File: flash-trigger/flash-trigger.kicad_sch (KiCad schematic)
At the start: 32 parts, among them J1 TRIG, J2 GND, Q1 NDS331N, SW1 PCM12, SW2 Bat Test, U1 74LV123, U2 BD48K27G

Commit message: Fixes and improvements
 * fix the preflash detection
 * clean the canon hot shoe schematics up
 * enlarge the hotshoe pcb and place two new mounting pins
 * change the battery low to a battery good detection
 * move the supervisor ic away from the hot shoe rail
 * use a longer pogo pin
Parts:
- removed U2: BD48K27G, Package_TO_SOT_SMD:SOT-23_Handsoldering, symbol Power_Management:BD48KxxG
- added J3, J4: GND, Connector_MillMax:0508_20mil, symbol Connector_Pin:Pin
- added U2: BD49KxxG, Package_TO_SOT_SMD:SOT-23_Handsoldering, symbol Power_Management:BD49KxxG
- D6: value RED -> GREEN
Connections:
- net +3V0: no longer D6.2 (A), U1.2 (B)
- net GND: now also D6.1 (K), U1.1 (A), J3.1 (Pin_1), J4.1 (Pin_1), U2.1 (GND)
- net TRIG: now also U1.2 (B); no longer U1.1 (A)
- net at R11.1: now also D6.2 (A); no longer D6.1 (K)
- net at R11.2: now also U2.2 (VOUT)
- net at R13.1, SW2.2: now also U2.3 (VDD)
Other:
- moved on the sheet: BT1, C2, C3, D6

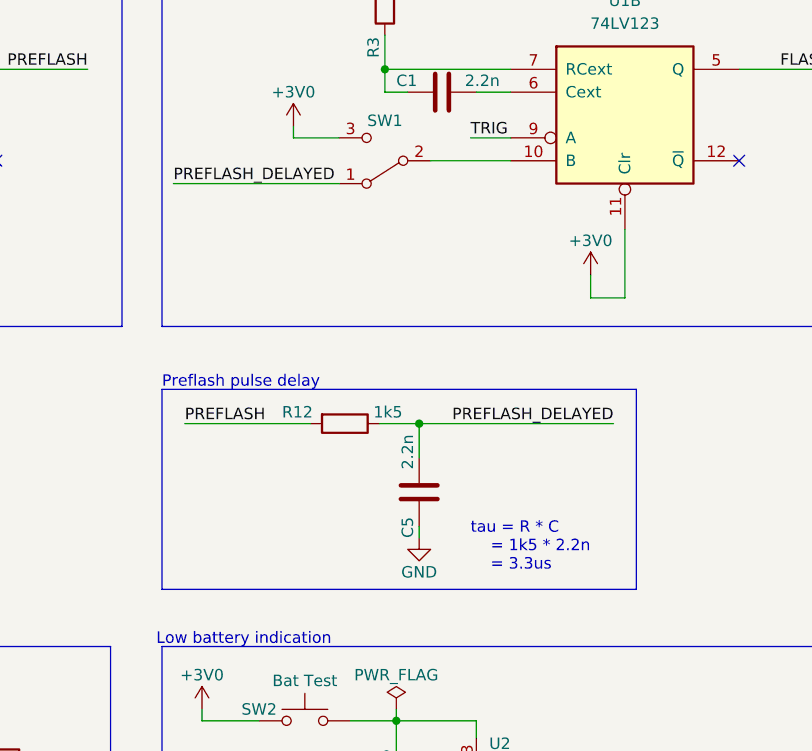
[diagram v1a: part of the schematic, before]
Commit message: flash-trigger: Drop RC circuit and improve layout
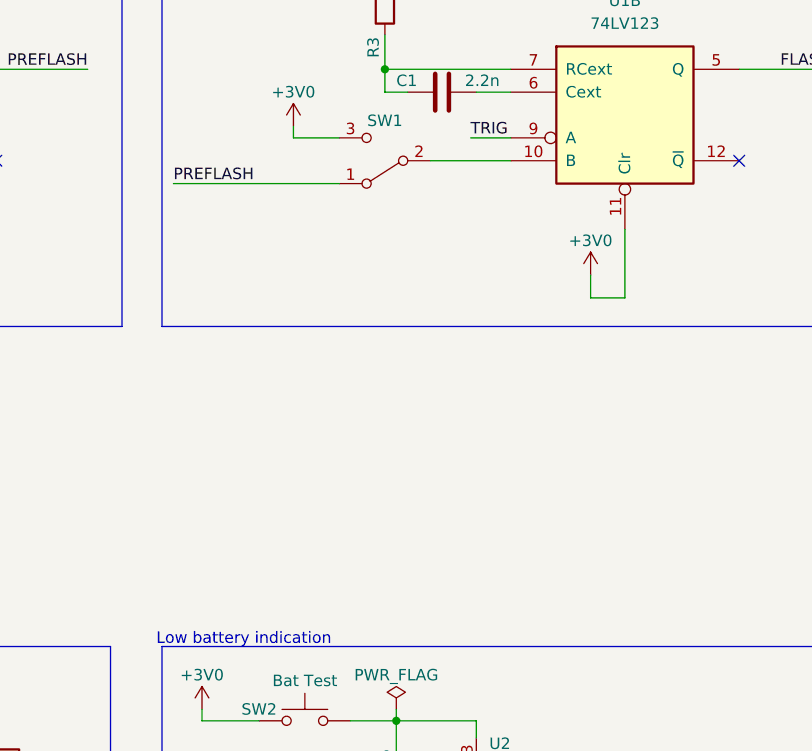
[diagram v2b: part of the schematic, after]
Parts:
- removed C5: 2.2n, Capacitor_SMD:C_0603_1608Metric_Pad1.08x0.95mm_HandSolder, symbol Device:C
- removed R12: 1k5, Resistor_SMD:R_0603_1608Metric_Pad0.98x0.95mm_HandSolder, symbol Device:R
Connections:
- net PREFLASH_DELAYED is gone; now on net PREFLASH: SW1.1 (A)
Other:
- note removed: "Preflash pulse delay"
- note removed: "tau = R * C = 1k5 * 2.2n = 3.3us"
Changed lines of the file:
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@@
   (junction (at 60.96 142.24) (diameter 0) (color 0 0 0 0)
-  )
-  (junction (at 142.875 93.98) (diameter 0) (color 0 0 0 0)
   )
   (junction (at 55.245 127.635) (diameter 0) (color 0 0 0 0)
@@
     (stroke (width 0) (type default) (color 0 0 0 0))
   )
-  (polyline (pts (xy 114.3 90.17) (xy 114.3 112.395))
-    (stroke (width 0) (type default) (color 0 0 0 0))
-  )
   (wire (pts (xy 245.11 49.53) (xy 245.11 57.15))
     (stroke (width 0) (type default) (color 0 0 0 0))
@@
     (stroke (width 0) (type default) (color 0 0 0 0))
   )
-  (wire (pts (xy 142.875 93.98) (xy 164.465 93.98))
-    (stroke (width 0) (type default) (color 0 0 0 0))
-  )
-  (wire (pts (xy 142.875 97.79) (xy 142.875 93.98))
-    (stroke (width 0) (type default) (color 0 0 0 0))
-  )
   (polyline (pts (xy 200.025 151.13) (xy 114.3 151.13))
     (stroke (width 0) (type default) (color 0 0 0 0))
@@
     (stroke (width 0) (type default) (color 0 0 0 0))
   )
-  (polyline (pts (xy 114.3 90.17) (xy 167.005 90.17))
-    (stroke (width 0) (type default) (color 0 0 0 0))
-  )
   (wire (pts (xy 79.375 77.47) (xy 79.375 80.01))
     (stroke (width 0) (type default) (color 0 0 0 0))
   )
-  (wire (pts (xy 142.875 105.41) (xy 142.875 106.68))
-    (stroke (width 0) (type default) (color 0 0 0 0))
-  )
   (wire (pts (xy 55.245 127.635) (xy 55.245 131.445))
     (stroke (width 0) (type default) (color 0 0 0 0))
@@
     (stroke (width 0) (type default) (color 0 0 0 0))
   )
-  (wire (pts (xy 138.43 93.98) (xy 142.875 93.98))
-    (stroke (width 0) (type default) (color 0 0 0 0))
-  )
   (wire (pts (xy 153.035 54.61) (xy 139.065 54.61))
     (stroke (width 0) (type default) (color 0 0 0 0))
@@
     (stroke (width 0) (type default) (color 0 0 0 0))
   )
-  (wire (pts (xy 116.84 93.98) (xy 130.81 93.98))
-    (stroke (width 0) (type default) (color 0 0 0 0))
-  )
   (polyline (pts (xy 15.24 195.58) (xy 99.06 195.58))
     (stroke (width 0) (type default) (color 0 0 0 0))
@@
     (stroke (width 0) (type default) (color 0 0 0 0))
   )
-  (polyline (pts (xy 114.3 112.395) (xy 167.005 112.395))
-    (stroke (width 0) (type default) (color 0 0 0 0))
-  )
   (wire (pts (xy 67.31 124.46) (xy 67.31 127.635))
     (stroke (width 0) (type default) (color 0 0 0 0))
@@
   )
   (wire (pts (xy 56.515 36.195) (xy 56.515 43.18))
-    (stroke (width 0) (type default) (color 0 0 0 0))
-  )
-  (polyline (pts (xy 167.005 90.17) (xy 167.005 112.395))
     (stroke (width 0) (type default) (color 0 0 0 0))
   )
@@
   )
   (text "Low battery indication" (at 113.665 118.745 0)
-    (effects (font (size 1.27 1.27)) (justify left bottom))
-  )
-  (text "tau = R * C\n    = 1k5 * 2.2n\n    = 3.3us" (at 148.59 110.49 0)
     (effects (font (size 1.27 1.27)) (justify left bottom))
   )
@@
     (effects (font (size 1.27 1.27)) (justify left bottom))
   )
-  (text "Preflash pulse delay" (at 114.3 90.17 0)
-    (effects (font (size 1.27 1.27)) (justify left bottom))
-  )
   (label "TRIG" (at 66.04 64.77 0)
     (effects (font (size 1.27 1.27)) (justify left bottom))
   )
-  (label "PREFLASH_DELAYED" (at 164.465 93.98 180)
-    (effects (font (size 1.27 1.27)) (justify right bottom))
-  )
   (label "TRIG" (at 148.59 62.23 0)
     (effects (font (size 1.27 1.27)) (justify left bottom))
   )
-  (label "PREFLASH_DELAYED" (at 115.57 67.31 0)
-    (effects (font (size 1.27 1.27)) (justify left bottom))
-  )
-  (label "PREFLASH" (at 116.84 93.98 0)
+  (label "PREFLASH" (at 115.57 67.31 0)
     (effects (font (size 1.27 1.27)) (justify left bottom))
   )
@@
     )
     (pin "1")
-  )
-  (symbol (lib_id "Device:R") (at 134.62 93.98 270) (unit 1)
-    (in_bom yes) (on_board yes)
-    (property "Reference" "R12" (id 0) (at 127.635 92.71 90)
-      (effects (font (size 1.27 1.27)) (justify left))
-    )
-    (property "Value" "1k5" (id 1) (at 137.795 92.71 90)
-      (effects (font (size 1.27 1.27)) (justify left))
-    )
-    (property "Footprint" "Resistor_SMD:R_0603_1608Metric_Pad0.98x0.95mm_HandSolder" (id 2) (at 134.62 92.202 90)
-      (effects (font (size 1.27 1.27)) hide)
-    )
-    (property "Datasheet" "~" (id 3) (at 134.62 93.98 0)
-      (effects (font (size 1.27 1.27)) hide)
-    )
-    (pin "1")
-    (pin "2")
   )
   (symbol (lib_id "Device:C") (at 62.865 57.15 270) (unit 1)
@@
     (pin "8")
   )
-  (symbol (lib_id "power:GND") (at 142.875 106.68 0) (unit 1)
-    (in_bom yes) (on_board yes)
-    (property "Reference" "#PWR02" (id 0) (at 142.875 113.03 0)
-      (effects (font (size 1.27 1.27)) hide)
-    )
-    (property "Value" "GND" (id 1) (at 142.875 110.49 0))
-    (property "Footprint" "" (id 2) (at 142.875 106.68 0)
-      (effects (font (size 1.27 1.27)) hide)
-    )
-    (property "Datasheet" "" (id 3) (at 142.875 106.68 0)
-      (effects (font (size 1.27 1.27)) hide)
-    )
-    (pin "1")
-  )
   (symbol (lib_id "Device:R") (at 224.79 74.93 90) (unit 1)
     (in_bom yes) (on_board yes)
@@
     )
     (pin "1")
-  )
-  (symbol (lib_id "Device:C") (at 142.875 101.6 0) (unit 1)
-    (in_bom yes) (on_board yes)
-    (property "Reference" "C5" (id 0) (at 141.605 106.68 90)
-      (effects (font (size 1.27 1.27)) (justify left))
-    )
-    (property "Value" "2.2n" (id 1) (at 141.605 99.06 90)
-      (effects (font (size 1.27 1.27)) (justify left))
-    )
-    (property "Footprint" "Capacitor_SMD:C_0603_1608Metric_Pad1.08x0.95mm_HandSolder" (id 2) (at 143.8402 105.41 0)
-      (effects (font (size 1.27 1.27)) hide)
-    )
-    (property "Datasheet" "~" (id 3) (at 142.875 101.6 0)
-      (effects (font (size 1.27 1.27)) hide)
-    )
-    (pin "1")
-    (pin "2")
   )
   (symbol (lib_id "power:GND") (at 194.945 138.43 0) (unit 1)
@@
       (reference "#PWR01") (unit 1) (value "GND") (footprint "")
     )
-    (path "/7525ff0d-7040-4ba5-9383-b2716010d0ab"
-      (reference "#PWR02") (unit 1) (value "GND") (footprint "")
-    )
     (path "/45240cf5-fa14-449b-8df8-95cb2ab631a1"
       (reference "#PWR03") (unit 1) (value "GND") (footprint "")
@@
       (reference "C4") (unit 1) (value "220n") (footprint "Capacitor_SMD:C_0603_1608Metric_Pad1.08x0.95mm_HandSolder")
     )
-    (path "/e5cffcd4-8c81-4263-b9d9-fc1257ee69ce"
-      (reference "C5") (unit 1) (value "2.2n") (footprint "Capacitor_SMD:C_0603_1608Metric_Pad1.08x0.95mm_HandSolder")
-    )
     (path "/412c51c3-a4b0-43de-9409-a8b70956267a"
       (reference "D1") (unit 1) (value "RED") (footprint "LED_THT:LED_D5.0mm_Horizontal_O3.81mm_Z3.0mm")
@@
       (reference "R11") (unit 1) (value "1k5") (footprint "Resistor_SMD:R_0603_1608Metric_Pad0.98x0.95mm_HandSolder")
     )
-    (path "/1aa0f7e1-6ed5-404c-ba9b-a644e163f5fb"
-      (reference "R12") (unit 1) (value "1k5") (footprint "Resistor_SMD:R_0603_1608Metric_Pad0.98x0.95mm_HandSolder")
-    )
     (path "/9efe46b7-7144-40b9-a143-1703b8afb1fc"

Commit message: Renumber RefDes and add OSHW logo and URL
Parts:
- renumbered C2 to C1, C3 to C2, C4 to C3, C1 to C4, R3 to R10, R13 to R12, R7 to R3, R8 to R4, R9 to R5, R4 to R6, R5 to R7, R6 to R8, R10 to R9
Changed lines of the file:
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@@
   (symbol (lib_id "Device:C") (at 62.865 57.15 270) (unit 1)
     (in_bom yes) (on_board yes)
-    (property "Reference" "C4" (id 0) (at 57.785 55.88 90)
+    (property "Reference" "C3" (id 0) (at 57.785 55.88 90)
       (effects (font (size 1.27 1.27)) (justify left))
     )
@@
   (symbol (lib_id "Device:C") (at 145.415 57.15 270) (unit 1)
     (in_bom yes) (on_board yes)
-    (property "Reference" "C1" (id 0) (at 140.335 55.88 90)
+    (property "Reference" "C4" (id 0) (at 140.335 55.88 90)
       (effects (font (size 1.27 1.27)) (justify left))
     )
@@
   (symbol (lib_id "Device:R") (at 260.35 60.96 0) (unit 1)
     (in_bom yes) (on_board yes)
-    (property "Reference" "R8" (id 0) (at 259.08 66.675 90)
+    (property "Reference" "R4" (id 0) (at 259.08 66.675 90)
       (effects (font (size 1.27 1.27)) (justify left))
     )
@@
   (symbol (lib_id "Device:R") (at 234.95 83.82 0) (unit 1)
     (in_bom yes) (on_board yes)
-    (property "Reference" "R5" (id 0) (at 233.68 89.535 90)
+    (property "Reference" "R7" (id 0) (at 233.68 89.535 90)
       (effects (font (size 1.27 1.27)) (justify left))
     )
@@
   (symbol (lib_id "Device:R") (at 224.79 74.93 90) (unit 1)
     (in_bom yes) (on_board yes)
-    (property "Reference" "R4" (id 0) (at 219.71 73.66 90))
+    (property "Reference" "R6" (id 0) (at 219.71 73.66 90))
     (property "Value" "22R" (id 1) (at 229.87 73.66 90))
     (property "Footprint" "Resistor_SMD:R_0603_1608Metric_Pad0.98x0.95mm_HandSolder" (id 2) (at 224.79 76.708 90)
@@
   (symbol (lib_id "Device:C") (at 60.96 135.255 0) (unit 1)
     (in_bom yes) (on_board yes)
-    (property "Reference" "C2" (id 0) (at 59.69 140.335 90)
+    (property "Reference" "C1" (id 0) (at 59.69 140.335 90)
       (effects (font (size 1.27 1.27)) (justify left))
     )
@@
   (symbol (lib_id "Device:C") (at 67.31 135.255 0) (unit 1)
     (in_bom yes) (on_board yes)
-    (property "Reference" "C3" (id 0) (at 66.04 140.335 90)
+    (property "Reference" "C2" (id 0) (at 66.04 140.335 90)
       (effects (font (size 1.27 1.27)) (justify left))
     )
@@
   (symbol (lib_id "Device:R") (at 140.335 136.525 0) (unit 1)
     (in_bom yes) (on_board yes)
-    (property "Reference" "R13" (id 0) (at 139.065 143.51 90)
+    (property "Reference" "R12" (id 0) (at 139.065 143.51 90)
       (effects (font (size 1.27 1.27)) (justify left))
     )
@@
   (symbol (lib_id "Device:R") (at 265.43 60.96 0) (unit 1)
     (in_bom yes) (on_board yes)
-    (property "Reference" "R9" (id 0) (at 264.16 66.675 90)
+    (property "Reference" "R5" (id 0) (at 264.16 66.675 90)
       (effects (font (size 1.27 1.27)) (justify left))
     )
@@
   (symbol (lib_id "Device:R") (at 255.27 60.96 0) (unit 1)
     (in_bom yes) (on_board yes)
-    (property "Reference" "R7" (id 0) (at 254 66.675 90)
+    (property "Reference" "R3" (id 0) (at 254 66.675 90)
       (effects (font (size 1.27 1.27)) (justify left))
     )
@@
   (symbol (lib_id "Device:R") (at 139.065 46.99 180) (unit 1)
     (in_bom yes) (on_board yes)
-    (property "Reference" "R3" (id 0) (at 137.795 53.34 90)
+    (property "Reference" "R10" (id 0) (at 137.795 53.34 90)
       (effects (font (size 1.27 1.27)) (justify right))
     )
@@
   (symbol (lib_id "Device:R") (at 35.56 46.99 180) (unit 1)
     (in_bom yes) (on_board yes)
-    (property "Reference" "R6" (id 0) (at 34.29 53.34 90)
+    (property "Reference" "R8" (id 0) (at 34.29 53.34 90)
       (effects (font (size 1.27 1.27)) (justify right))
     )
@@
   (symbol (lib_id "Device:R") (at 56.515 46.99 180) (unit 1)
     (in_bom yes) (on_board yes)
-    (property "Reference" "R10" (id 0) (at 55.245 53.34 90)
+    (property "Reference" "R9" (id 0) (at 55.245 53.34 90)
       (effects (font (size 1.27 1.27)) (justify right))
     )
@@
       (reference "BT1") (unit 1) (value "CR2032") (footprint "Battery_Keystone:BatteryHolder_Keystone_2899_1x2032")
     )
+    (path "/8603793e-c9cb-4fd1-8bc3-86943498fd16"
+      (reference "C1") (unit 1) (value "10n") (footprint "Capacitor_SMD:C_0603_1608Metric_Pad1.08x0.95mm_HandSolder")
+    )
+    (path "/8eb124df-87e9-488c-9f2f-f3f6fb560814"
+      (reference "C2") (unit 1) (value "47u") (footprint "Capacitor_SMD:C_0805_2012Metric_Pad1.18x1.45mm_HandSolder")
+    )
+    (path "/21972450-4e20-4965-b341-d4d19cc02663"
+      (reference "C3") (unit 1) (value "220n") (footprint "Capacitor_SMD:C_0603_1608Metric_Pad1.08x0.95mm_HandSolder")
+    )
     (path "/24ebdac6-ab66-4cce-b6aa-732e2f68d56b"
-      (reference "C1") (unit 1) (value "2.2n") (footprint "Capacitor_SMD:C_0603_1608Metric_Pad1.08x0.95mm_HandSolder")
-    )
-    (path "/8603793e-c9cb-4fd1-8bc3-86943498fd16"
-      (reference "C2") (unit 1) (value "10n") (footprint "Capacitor_SMD:C_0603_1608Metric_Pad1.08x0.95mm_HandSolder")
-    )
-    (path "/8eb124df-87e9-488c-9f2f-f3f6fb560814"
-      (reference "C3") (unit 1) (value "47u") (footprint "Capacitor_SMD:C_0805_2012Metric_Pad1.18x1.45mm_HandSolder")
-    )
-    (path "/21972450-4e20-4965-b341-d4d19cc02663"
-      (reference "C4") (unit 1) (value "220n") (footprint "Capacitor_SMD:C_0603_1608Metric_Pad1.08x0.95mm_HandSolder")
+      (reference "C4") (unit 1) (value "2.2n") (footprint "Capacitor_SMD:C_0603_1608Metric_Pad1.08x0.95mm_HandSolder")
     )
     (path "/412c51c3-a4b0-43de-9409-a8b70956267a"
@@
       (reference "R2") (unit 1) (value "22R") (footprint "Resistor_SMD:R_0603_1608Metric_Pad0.98x0.95mm_HandSolder")
     )
+    (path "/bf096572-a861-4ef8-aec4-bc1550228472"
+      (reference "R3") (unit 1) (value "22R") (footprint "Resistor_SMD:R_0603_1608Metric_Pad0.98x0.95mm_HandSolder")
+    )
+    (path "/63f201b4-73a0-4dbc-9648-532cc3a3f3de"
+      (reference "R4") (unit 1) (value "22R") (footprint "Resistor_SMD:R_0603_1608Metric_Pad0.98x0.95mm_HandSolder")
+    )
+    (path "/abb0e412-d476-4a0a-924c-17a8293a1fb7"
+      (reference "R5") (unit 1) (value "22R") (footprint "Resistor_SMD:R_0603_1608Metric_Pad0.98x0.95mm_HandSolder")
+    )
+    (path "/79182a0c-8101-41eb-a496-d7282fc3a91e"
+      (reference "R6") (unit 1) (value "22R") (footprint "Resistor_SMD:R_0603_1608Metric_Pad0.98x0.95mm_HandSolder")
+    )
+    (path "/64a89449-ebf7-4ac3-92a7-dac0a82d20c9"
+      (reference "R7") (unit 1) (value "100k") (footprint "Resistor_SMD:R_0603_1608Metric_Pad0.98x0.95mm_HandSolder")
+    )
+    (path "/f33d470f-c682-472a-a000-d76a8f98048e"
+      (reference "R8") (unit 1) (value "100k") (footprint "Resistor_SMD:R_0603_1608Metric_Pad0.98x0.95mm_HandSolder")
+    )
+    (path "/fb29be56-2f4e-4e5f-b2f7-ab15c6a779be"
+      (reference "R9") (unit 1) (value "1M") (footprint "Resistor_SMD:R_0603_1608Metric_Pad0.98x0.95mm_HandSolder")
+    )
     (path "/c4e9f0c6-b89b-44ff-bd0e-6feb2e01b859"
-      (reference "R3") (unit 1) (value "100k") (footprint "Resistor_SMD:R_0603_1608Metric_Pad0.98x0.95mm_HandSolder")
-    )
-    (path "/79182a0c-8101-41eb-a496-d7282fc3a91e"
-      (reference "R4") (unit 1) (value "22R") (footprint "Resistor_SMD:R_0603_1608Metric_Pad0.98x0.95mm_HandSolder")
-    )
-    (path "/64a89449-ebf7-4ac3-92a7-dac0a82d20c9"
-      (reference "R5") (unit 1) (value "100k") (footprint "Resistor_SMD:R_0603_1608Metric_Pad0.98x0.95mm_HandSolder")
-    )
-    (path "/f33d470f-c682-472a-a000-d76a8f98048e"
-      (reference "R6") (unit 1) (value "100k") (footprint "Resistor_SMD:R_0603_1608Metric_Pad0.98x0.95mm_HandSolder")
-    )
-    (path "/bf096572-a861-4ef8-aec4-bc1550228472"
-      (reference "R7") (unit 1) (value "22R") (footprint "Resistor_SMD:R_0603_1608Metric_Pad0.98x0.95mm_HandSolder")
-    )
-    (path "/63f201b4-73a0-4dbc-9648-532cc3a3f3de"
-      (reference "R8") (unit 1) (value "22R") (footprint "Resistor_SMD:R_0603_1608Metric_Pad0.98x0.95mm_HandSolder")
-    )
-    (path "/abb0e412-d476-4a0a-924c-17a8293a1fb7"
-      (reference "R9") (unit 1) (value "22R") (footprint "Resistor_SMD:R_0603_1608Metric_Pad0.98x0.95mm_HandSolder")
-    )
-    (path "/fb29be56-2f4e-4e5f-b2f7-ab15c6a779be"
-      (reference "R10") (unit 1) (value "1M") (footprint "Resistor_SMD:R_0603_1608Metric_Pad0.98x0.95mm_HandSolder")
+      (reference "R10") (unit 1) (value "100k") (footprint "Resistor_SMD:R_0603_1608Metric_Pad0.98x0.95mm_HandSolder")
     )
     (path "/d11af2bb-e9e9-4c44-815f-13989478e9fd"
@@
     )
     (path "/9efe46b7-7144-40b9-a143-1703b8afb1fc"
-      (reference "R13") (unit 1) (value "1k5") (footprint "Resistor_SMD:R_0603_1608Metric_Pad0.98x0.95mm_HandSolder")
+      (reference "R12") (unit 1) (value "1k5") (footprint "Resistor_SMD:R_0603_1608Metric_Pad0.98x0.95mm_HandSolder")
     )
     (path "/0a0cefdf-d7a4-4421-b396-cfd9b707c670"

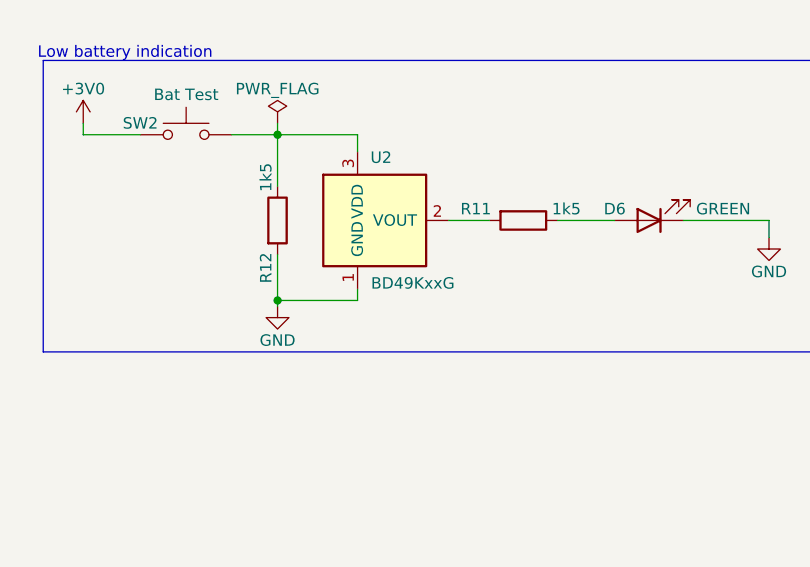
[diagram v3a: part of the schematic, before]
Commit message: flash-trigger: replace BD49KxxG with BD49K27G
We use a 2.7V voltage supervisor.
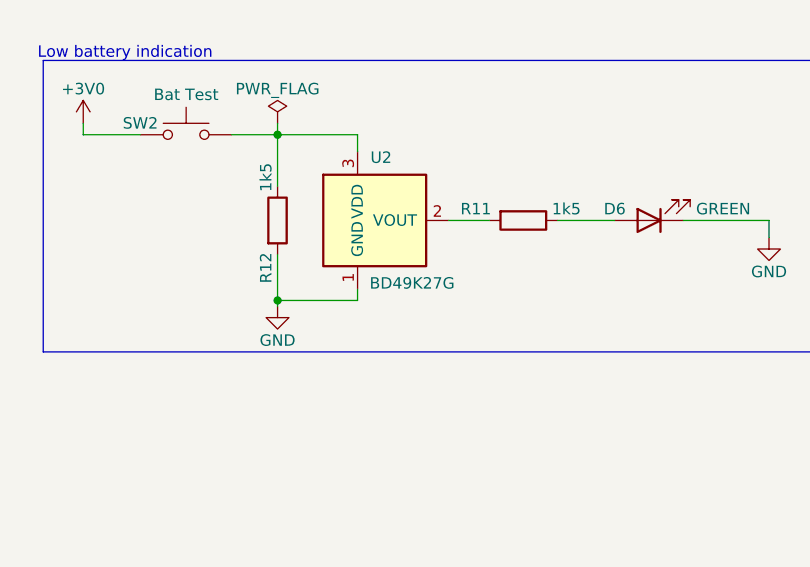
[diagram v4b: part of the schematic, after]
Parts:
- U2: value BD49KxxG -> BD49K27G
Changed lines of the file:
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@@
       (effects (font (size 1.27 1.27)) (justify right))
     )
-    (property "Value" "BD49KxxG" (id 1) (at 160.02 143.51 0)
+    (property "Value" "BD49K27G" (id 1) (at 160.02 143.51 0)
       (effects (font (size 1.27 1.27)) (justify right))
     )
@@
     )
     (path "/d8838f96-bcbf-4cb1-9b90-0640aa8aa469"
-      (reference "U2") (unit 1) (value "BD49KxxG") (footprint "Package_TO_SOT_SMD:SOT-23_Handsoldering")
-    )
-  )
+      (reference "U2") (unit 1) (value "BD49K27G") (footprint "Package_TO_SOT_SMD:SOT-23_Handsoldering")
+    )
+  )
